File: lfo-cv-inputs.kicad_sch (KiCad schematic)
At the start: 43 parts

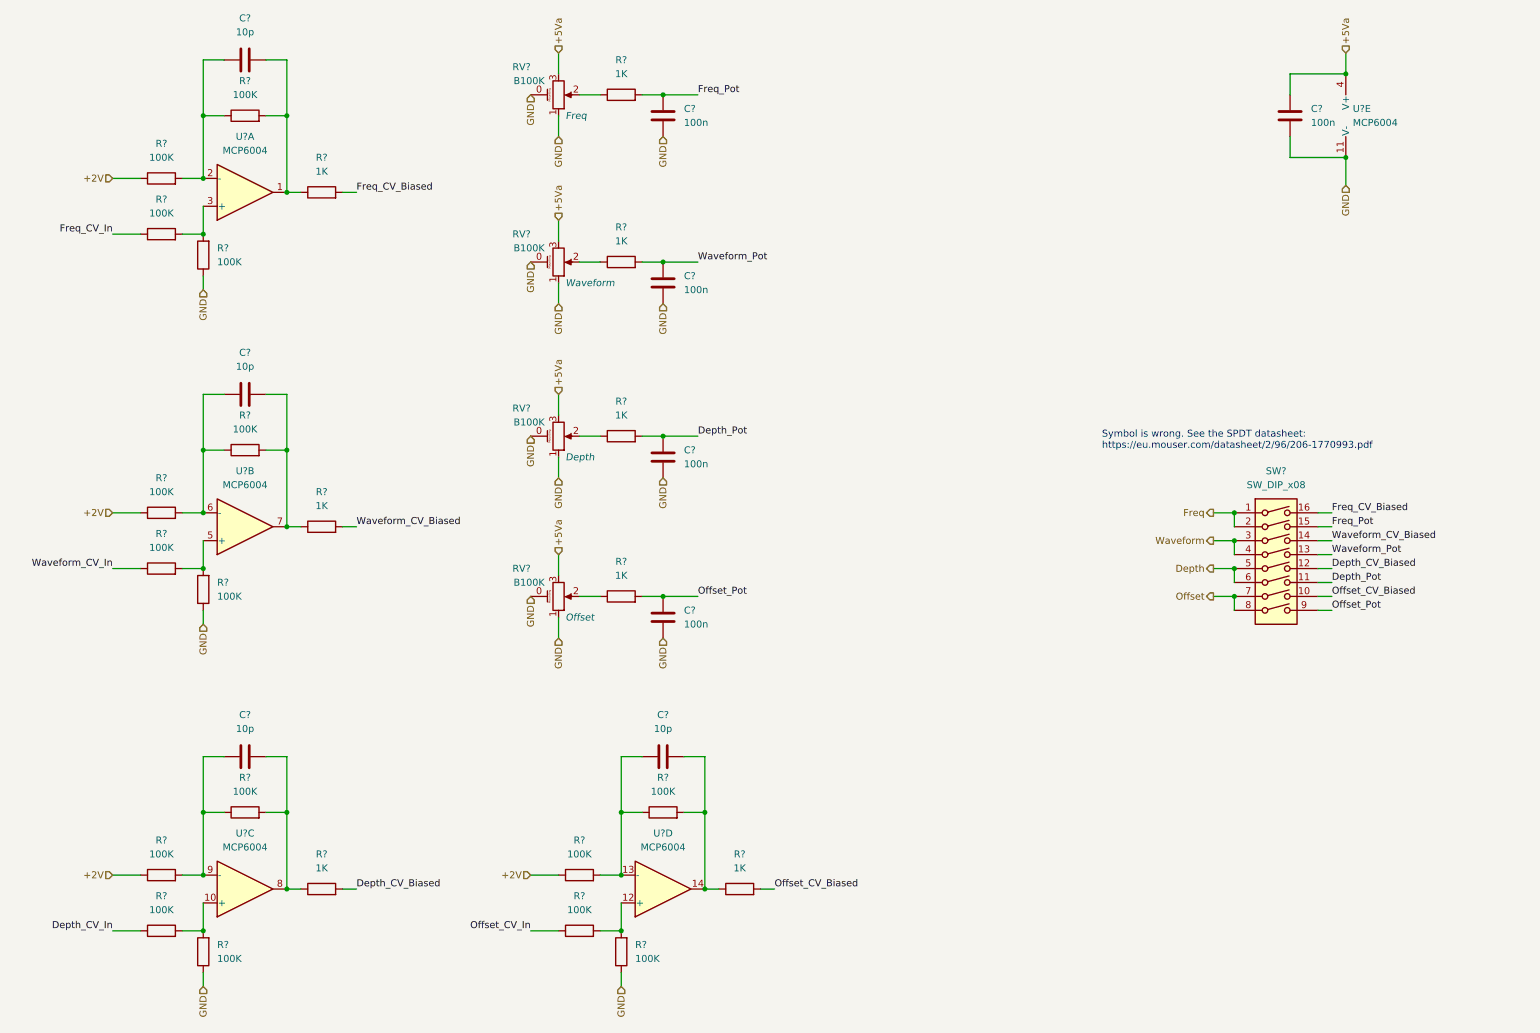
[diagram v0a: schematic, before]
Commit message: LFO schem capture done / replace r2r opamps
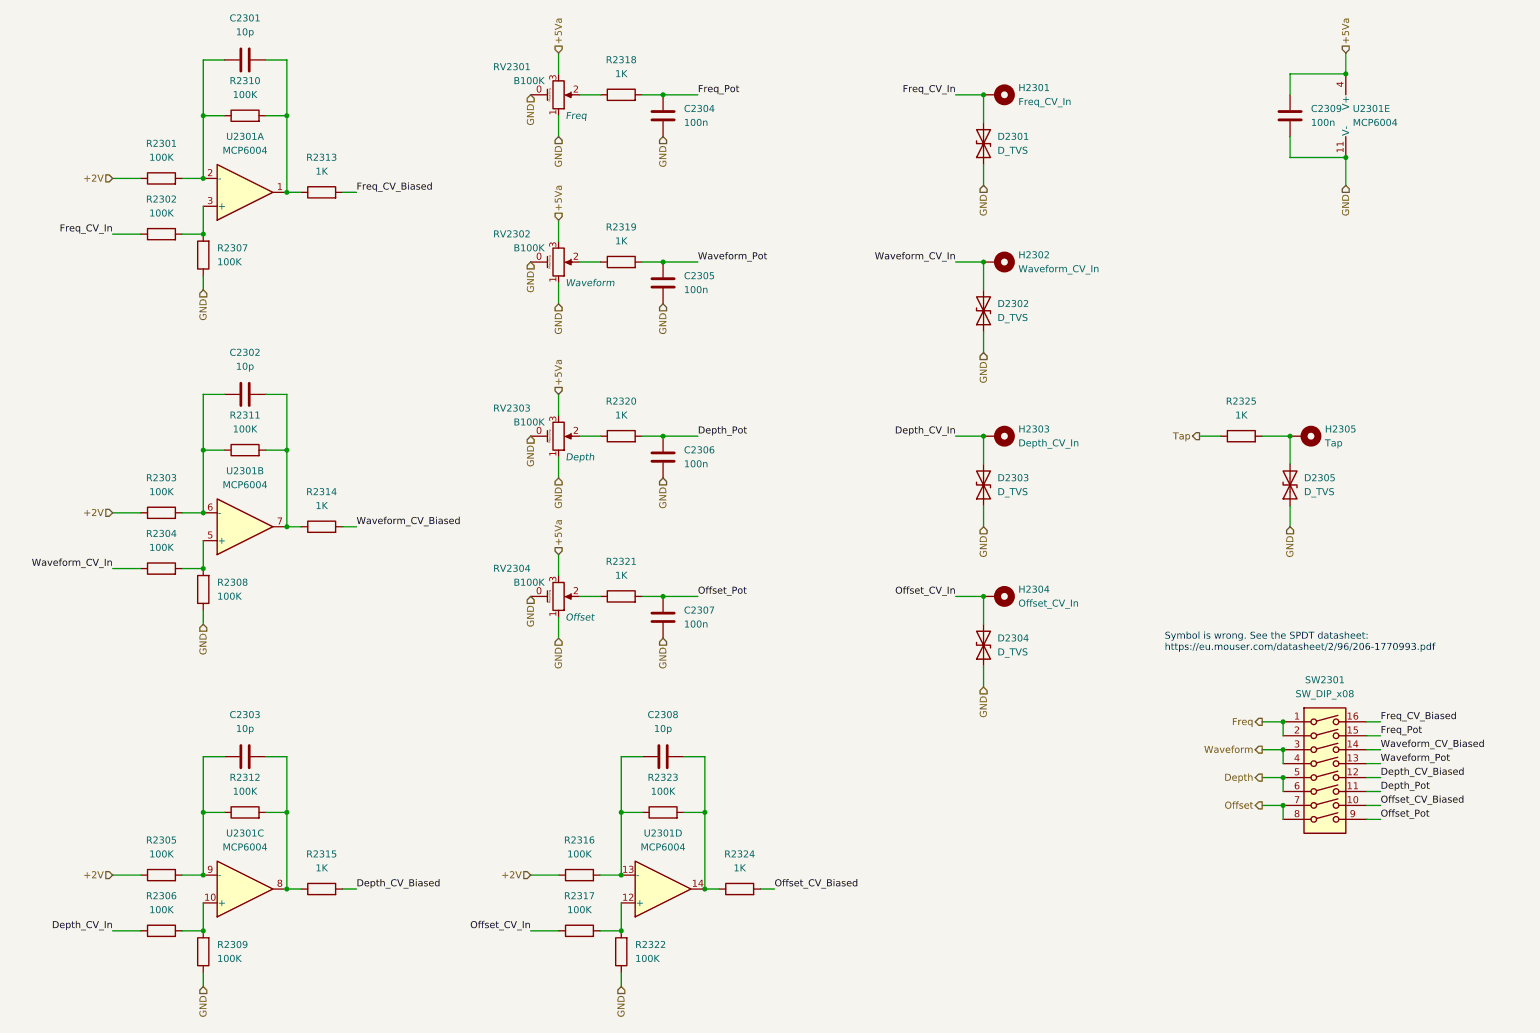
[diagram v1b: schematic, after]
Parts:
- added D2301, D2302, D2303, D2304, D2305: D_TVS, Diode_SMD:D_SOD-323_HandSoldering, symbol Device:D_TVS
- added H2301: Freq_CV_In, MountingHole:MountingHole_4.3mm_M4_Pad_TopBottom, symbol Mechanical:MountingHole_Pad
- added H2302: Waveform_CV_In, MountingHole:MountingHole_4.3mm_M4_Pad_TopBottom, symbol Mechanical:MountingHole_Pad
- added H2303: Depth_CV_In, MountingHole:MountingHole_4.3mm_M4_Pad_TopBottom, symbol Mechanical:MountingHole_Pad
- added H2304: Offset_CV_In, MountingHole:MountingHole_4.3mm_M4_Pad_TopBottom, symbol Mechanical:MountingHole_Pad
- added H2305: Tap, MountingHole:MountingHole_4.3mm_M4_Pad_TopBottom, symbol Mechanical:MountingHole_Pad
- added R2325: 1K, Resistor_SMD:R_0603_1608Metric_Pad0.98x0.95mm_HandSolder, symbol Device:R
- SW2301: renamed from SW?; footprint (none) -> Button_Switch_THT:SW_DIP_SPSTx08_Slide_9.78x22.5mm_W7.62mm_P2.54mm
- gave numbers to parts that had none: 38
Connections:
- net Depth_CV_In: now also D2303.2 (A2), H2303.1
- net Freq_CV_In: now also D2301.2 (A2), H2301.1
- net GND: now also D2301.1 (A1), D2302.1 (A1), D2303.1 (A1), D2304.1 (A1), D2305.1 (A1)
- net Offset_CV_In: now also D2304.2 (A2), H2304.1
- net Waveform_CV_In: now also D2302.2 (A2), H2302.1
- new net: D2305.2 (A2), H2305.1, R2325.2
- new net Tap: R2325.1
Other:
- moved on the sheet: SW2301

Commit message: LFO layout down
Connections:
- net at C2303.1, R2305.2, R2312.1: now also U2301.6 (-); no longer U2301.9 (-)
- net at C2303.2, R2312.2, R2315.1: now also U2301.7; no longer U2301.8
- net at C2302.1, R2303.2, R2311.1: now also U2301.9 (-); no longer U2301.6 (-)
- net at C2302.2, R2311.2, R2314.1: now also U2301.8; no longer U2301.7
- net at R2317.2, R2322.2: now also U2301.3 (+); no longer U2301.12 (+)
- net at C2308.1, R2316.2, R2323.1: now also U2301.2 (-); no longer U2301.13 (-)
- net at C2308.2, R2323.2, R2324.1: now also U2301.1; no longer U2301.14
- net at C2301.2, R2310.2, R2313.1: now also U2301.14; no longer U2301.1
- net at C2301.1, R2301.2, R2310.1: now also U2301.13 (-); no longer U2301.2 (-)
- net at R2302.2, R2307.2: now also U2301.12 (+); no longer U2301.3 (+)
- net at R2304.2, R2308.2: now also U2301.10 (+); no longer U2301.5 (+)
- net at R2306.2, R2309.2: now also U2301.5 (+); no longer U2301.10 (+)
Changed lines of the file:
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@@
     (pin "2")
   )
-  (symbol (lib_id "Amplifier_Operational:MCP6004") (at 133.35 172.72 0) (mirror x) (unit 4)
+  (symbol (lib_id "Amplifier_Operational:MCP6004") (at 133.35 172.72 0) (mirror x) (unit 1)
     (in_bom yes) (on_board yes) (fields_autoplaced)
     (property "Reference" "U2301" (id 0) (at 133.35 162.56 0))
@@
     (pin "2")
   )
-  (symbol (lib_id "Amplifier_Operational:MCP6004") (at 57.15 45.72 0) (mirror x) (unit 1)
+  (symbol (lib_id "Amplifier_Operational:MCP6004") (at 57.15 45.72 0) (mirror x) (unit 4)
     (in_bom yes) (on_board yes) (fields_autoplaced)
     (property "Reference" "U2301" (id 0) (at 57.15 35.56 0))
@@
     (pin "2")
   )
-  (symbol (lib_id "Amplifier_Operational:MCP6004") (at 57.15 106.68 0) (mirror x) (unit 2)
+  (symbol (lib_id "Amplifier_Operational:MCP6004") (at 57.15 106.68 0) (mirror x) (unit 3)
     (in_bom yes) (on_board yes) (fields_autoplaced)
     (property "Reference" "U2301" (id 0) (at 57.15 96.52 0))
@@
     (pin "2")
   )
-  (symbol (lib_id "Amplifier_Operational:MCP6004") (at 57.15 172.72 0) (mirror x) (unit 3)
+  (symbol (lib_id "Amplifier_Operational:MCP6004") (at 57.15 172.72 0) (mirror x) (unit 2)
     (in_bom yes) (on_board yes) (fields_autoplaced)
     (property "Reference" "U2301" (id 0) (at 57.15 162.56 0))

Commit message: Add JLC parts numbers
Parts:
- C2301, C2302, C2303, C2308: LCSC (none) -> C91367; Role (none) -> opamp-filter
- C2304, C2305, C2306, C2307: LCSC (none) -> C519438; Role (none) -> cv-filter
- C2309: LCSC (none) -> C497032; Role (none) -> ic-bypass
- D2301, D2302, D2303, D2304, D2305: LCSC (none) -> C20936
- R2301, R2302, R2303, R2304, R2305, R2306, R2307, R2308, R2309, R2310, R2311, R2312, R2316, R2317, R2322, R2323: LCSC (none) -> C14675
- R2313, R2314, R2315, R2318, R2319, R2320, R2321, R2324, R2325: LCSC (none) -> C2907002
- U2301: LCSC (none) -> C7378
